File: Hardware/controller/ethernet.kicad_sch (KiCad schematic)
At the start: 33 parts

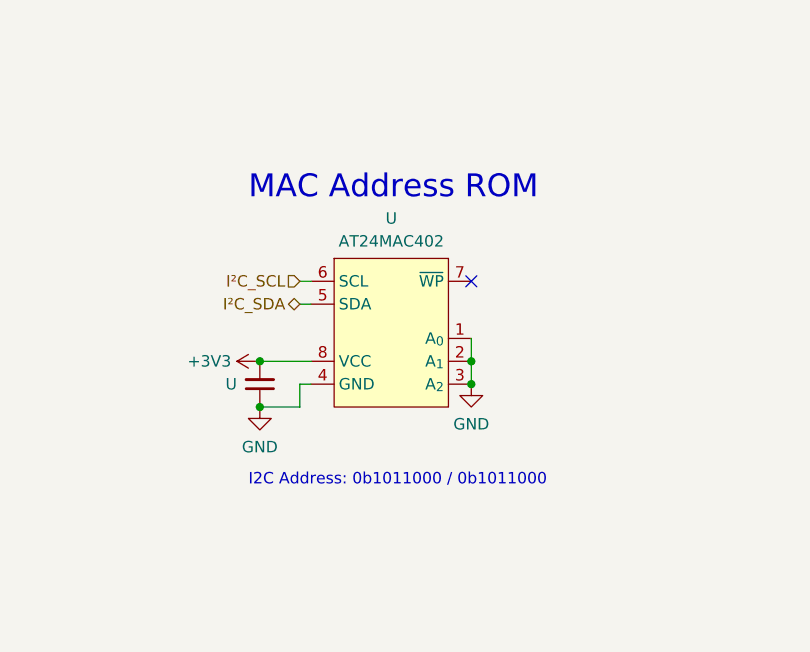
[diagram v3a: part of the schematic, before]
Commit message: hw: start working on rev4 controller
- removed SPI for display, and the associated SPI mux nonsense, and any
  superfluous resistors for pull-ups

- removed MAC address EEPROM

- start adding i2c RTC (which will also contain EEPROM with the MAC of
  the system, lol)

- start moving some components from bottom to top side of board

- tweaked positions of some mains voltage traces

- increased values of power indicator LED's current dropping resistors

- take 3V3 from SoM rather than generate it ourselves
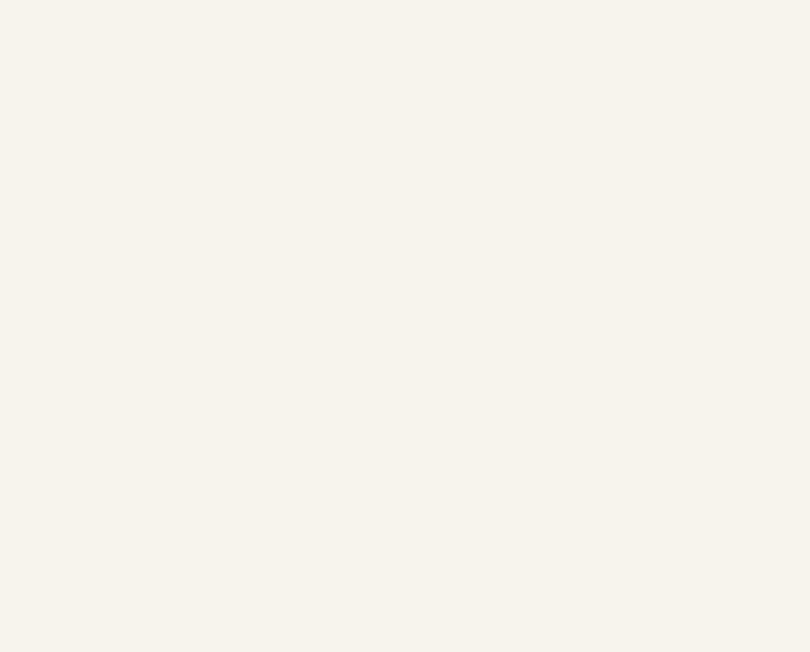
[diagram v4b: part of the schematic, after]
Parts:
- removed U: (no value), symbol Device:C_Small
- removed U: AT24MAC402, Package_SO:TSSOP-8_4.4x3mm_P0.65mm, symbol programmable-load:AT24MAC402
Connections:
- no-connect marks 2 -> 1
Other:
- note removed: "I2C Address: 0b1011000 / 0b1011000"
- note removed: "MAC Address ROM"
- title: (none) -> Programmable Load Controller
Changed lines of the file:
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@@
 (kicad_sch (version 20220404) (generator eeschema)
   (paper "A4")
+  (title_block
+    (title "Programmable Load Controller")
+    (date "2022-06-28")
+    (rev "4")
+  )
   (junction (at 34.29 175.26) (diameter 0) (color 0 0 0 0)
   )
@@
   (junction (at 42.545 125.095) (diameter 0) (color 0 0 0 0)
   )
-  (junction (at 185.42 144.78) (diameter 0) (color 0 0 0 0)
-  )
   (junction (at 89.535 171.45) (diameter 0) (color 0 0 0 0)
   )
@@
   (junction (at 52.705 125.095) (diameter 0) (color 0 0 0 0)
   )
-  (junction (at 208.915 147.32) (diameter 0) (color 0 0 0 0)
-  )
-  (junction (at 185.42 149.86) (diameter 0) (color 0 0 0 0)
-  )
   (junction (at 146.05 27.305) (diameter 0) (color 0 0 0 0)
   )
@@
   (junction (at 34.29 183.515) (diameter 0) (color 0 0 0 0)
   )
-  (junction (at 208.915 144.78) (diameter 0) (color 0 0 0 0)
-  )
   (junction (at 219.075 69.215) (diameter 0) (color 0 0 0 0)
   )
@@
   (junction (at 250.19 69.215) (diameter 0) (color 0 0 0 0)
   )
-  (no_connect (at 208.915 135.89))
   (no_connect (at 106.68 83.82))
   (wire (pts (xy 19.05 175.26) (xy 29.21 175.26))
@@
     (stroke (width 0) (type default))
   )
-  (wire (pts (xy 208.915 142.24) (xy 208.915 144.78))
-    (stroke (width 0) (type default))
-  )
   (wire (pts (xy 105.41 66.04) (xy 106.68 66.04))
     (stroke (width 0) (type default))
@@
     (stroke (width 0) (type default))
   )
-  (wire (pts (xy 208.915 144.78) (xy 208.915 147.32))
-    (stroke (width 0) (type default))
-  )
   (wire (pts (xy 75.565 179.07) (xy 89.535 179.07))
     (stroke (width 0) (type default))
@@
     (stroke (width 0) (type default))
   )
-  (wire (pts (xy 189.865 135.89) (xy 191.135 135.89))
-    (stroke (width 0) (type default))
-  )
   (wire (pts (xy 95.885 58.42) (xy 106.68 58.42))
     (stroke (width 0) (type default))
@@
     (stroke (width 0) (type default))
   )
-  (wire (pts (xy 185.42 144.78) (xy 191.135 144.78))
-    (stroke (width 0) (type default))
-  )
   (wire (pts (xy 19.05 118.11) (xy 19.05 116.84))
     (stroke (width 0) (type default))
@@
     (stroke (width 0) (type default))
   )
-  (wire (pts (xy 185.42 149.86) (xy 189.865 149.86))
-    (stroke (width 0) (type default))
-  )
   (wire (pts (xy 105.41 60.96) (xy 106.68 60.96))
     (stroke (width 0) (type default))
@@
     (stroke (width 0) (type default))
   )
-  (wire (pts (xy 189.865 149.86) (xy 189.865 147.32))
-    (stroke (width 0) (type default))
-  )
   (wire (pts (xy 42.545 116.84) (xy 52.705 116.84))
     (stroke (width 0) (type default))
@@
     (stroke (width 0) (type default))
   )
-  (wire (pts (xy 189.865 138.43) (xy 191.135 138.43))
-    (stroke (width 0) (type default))
-  )
   (wire (pts (xy 86.995 55.88) (xy 88.265 55.88))
     (stroke (width 0) (type default))
@@
   )
   (wire (pts (xy 75.565 177.8) (xy 75.565 179.07))
-    (stroke (width 0) (type default))
-  )
-  (wire (pts (xy 189.865 147.32) (xy 191.135 147.32))
     (stroke (width 0) (type default))
   )
@@
     (effects (font (size 2.54 2.54)) (justify left bottom))
   )
-  (text "I2C Address: 0b1011000 / 0b1011000" (at 184.15 158.75 0)
-    (effects (font (size 1.27 1.27)) (justify left bottom))
-  )
-  (text "MAC Address ROM" (at 184.15 127 0)
-    (effects (font (size 2.54 2.54)) (justify left bottom))
-  )
   (text "No resistors needed: have internal 10K pull-ups" (at 104.14 130.175 0)
     (effects (font (size 1.27 1.27)) (justify left bottom))
@@
     (effects (font (size 1.27 1.27)) (justify right))
   )
-  (hierarchical_label "I²C_SCL " (shape input) (at 189.865 135.89 180) (fields_autoplaced)
-    (effects (font (size 1.27 1.27)) (justify right))
-  )
   (hierarchical_label "CLKIN" (shape input) (at 91.44 81.28 180) (fields_autoplaced)
     (effects (font (size 1.27 1.27)) (justify right))
   )
   (hierarchical_label "~{IRQ}" (shape output) (at 105.41 76.2 180) (fields_autoplaced)
-    (effects (font (size 1.27 1.27)) (justify right))
-  )
-  (hierarchical_label "I²C_SDA" (shape bidirectional) (at 189.865 138.43 180) (fields_autoplaced)
     (effects (font (size 1.27 1.27)) (justify right))
   )
@@
     (pin "2")
   )
-  (symbol (lib_id "power:+3V3") (at 185.42 144.78 90) (unit 1)
-    (in_bom yes) (on_board yes)
-    (default_instance (reference "#PWR") (unit 1) (value "+3V3") (footprint ""))
-    (property "Reference" "#PWR" (id 0) (at 189.23 144.78 0)
-      (effects (font (size 1.27 1.27)) hide)
-    )
-    (property "Value" "+3V3" (id 1) (at 182.245 144.78 90)
-      (effects (font (size 1.27 1.27)) (justify left))
-    )
-    (property "Footprint" "" (id 2) (at 185.42 144.78 0)
-      (effects (font (size 1.27 1.27)) hide)
-    )
-    (property "Datasheet" "" (id 3) (at 185.42 144.78 0)
-      (effects (font (size 1.27 1.27)) hide)
-    )
-    (pin "1")
-  )
   (symbol (lib_id "Device:R_Small") (at 31.75 191.135 90) (unit 1)
     (in_bom yes) (on_board yes)
@@
     (pin "2")
   )
-  (symbol (lib_id "Device:C_Small") (at 185.42 147.32 0) (mirror x) (unit 1)
-    (in_bom yes) (on_board yes)
-    (default_instance (reference "U") (unit 1) (value "") (footprint ""))
-    (property "Reference" "U" (id 0) (at 182.88 147.32 0)
-      (effects (font (size 1.27 1.27)) (justify right))
-    )
-    (property "Value" "" (id 1) (at 182.88 149.86 0)
-      (effects (font (size 1.27 1.27)) (justify right))
-    )
-    (property "Footprint" "" (id 2) (at 185.42 147.32 0)
-      (effects (font (size 1.27 1.27)) hide)
-    )
-    (property "Datasheet" "~" (id 3) (at 185.42 147.32 0)
-      (effects (font (size 1.27 1.27)) hide)
-    )
-    (property "MPN" "" (id 4) (at 185.42 147.32 0)
-      (effects (font (size 1.27 1.27)) hide)
-    )
-    (pin "1")
-    (pin "2")
-  )
   (symbol (lib_id "Device:C_Small") (at 221.615 60.325 90) (unit 1)
     (in_bom yes) (on_board yes) (fields_autoplaced)
@@
     (pin "1")
   )
-  (symbol (lib_id "programmable-load:AT24MAC402") (at 200.025 133.35 0) (unit 1)
-    (in_bom yes) (on_board yes)
-    (default_instance (reference "U") (unit 1) (value "AT24MAC402") (footprint "Package_SO:TSSOP-8_4.4x3mm_P0.65mm"))
-    (property "Reference" "U" (id 0) (at 200.025 128.905 0)
-      (effects (font (size 1.27 1.27)))
-    )
-    (property "Value" "AT24MAC402" (id 1) (at 200.025 131.445 0)
-      (effects (font (size 1.27 1.27)))
-    )
-    (property "Footprint" "Package_SO:TSSOP-8_4.4x3mm_P0.65mm" (id 2) (at 200.025 124.46 0)
-      (effects (font (size 1.27 1.27)) hide)
-    )
-    (property "Datasheet" "https://www.mouser.com/datasheet/2/268/Atmel_8807_SEEPROM_AT24MAC402_602_Datasheet-1368957.pdf" (id 3) (at 200.025 127 0)
-      (effects (font (size 1.27 1.27)) hide)
-    )
-    (property "MPN" "AT24MAC402-XHM-T" (id 4) (at 200.025 133.35 0)
-      (effects (font (size 1.27 1.27)) hide)
-    )
-    (pin "1")
-    (pin "2")
-    (pin "3")
-    (pin "4")
-    (pin "5")
-    (pin "6")
-    (pin "7")
-    (pin "8")
-  )
   (symbol (lib_id "programmable-load:+3V3A") (at 19.05 116.84 0) (unit 1)
     (in_bom yes) (on_board yes)
@@
     (pin "1")
     (pin "2")
-  )
-  (symbol (lib_id "power:GND") (at 185.42 149.86 0) (unit 1)
-    (in_bom yes) (on_board yes)
-    (default_instance (reference "#PWR") (unit 1) (value "GND") (footprint ""))
-    (property "Reference" "#PWR" (id 0) (at 185.42 156.21 0)
-      (effects (font (size 1.27 1.27)) hide)
-    )
-    (property "Value" "GND" (id 1) (at 185.42 154.305 0)
-      (effects (font (size 1.27 1.27)))
-    )
-    (property "Footprint" "" (id 2) (at 185.42 149.86 0)
-      (effects (font (size 1.27 1.27)) hide)
-    )
-    (property "Datasheet" "" (id 3) (at 185.42 149.86 0)
-      (effects (font (size 1.27 1.27)) hide)
-    )
-    (pin "1")
   )
   (symbol (lib_id "Device:R_Small") (at 247.65 38.735 270) (mirror x) (unit 1)
@@
     (pin "5")
   )
-  (symbol (lib_id "power:GND") (at 208.915 147.32 0) (unit 1)
-    (in_bom yes) (on_board yes)
-    (default_instance (reference "#PWR") (unit 1) (value "GND") (footprint ""))
-    (property "Reference" "#PWR" (id 0) (at 208.915 153.67 0)
-      (effects (font (size 1.27 1.27)) hide)
-    )
-    (property "Value" "GND" (id 1) (at 208.915 151.765 0)
-      (effects (font (size 1.27 1.27)))
-    )
-    (property "Footprint" "" (id 2) (at 208.915 147.32 0)
-      (effects (font (size 1.27 1.27)) hide)
-    )
-    (property "Datasheet" "" (id 3) (at 208.915 147.32 0)
-      (effects (font (size 1.27 1.27)) hide)
-    )
-    (pin "1")
-  )
   (symbol (lib_id "power:GND") (at 146.05 33.655 0) (unit 1)

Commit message: hw: add charger for RTC
- added RTC supercapacitor

- added the charging circuit for the RTC (with adjustment for voltage
  and all that fun stuff) based around a bonus linear regulator for the
  supercap

- minor tweaks all around: add more JLCPCB part numbers and fixed some
  footprints for some components
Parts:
- R: JLCPCB (none) -> C25804
- R: JLCPCB (none) -> C23140
- U: JLCPCB (none) -> C4190
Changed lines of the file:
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@@
+      (effects (font (size 1.27 1.27)) hide)
+    )
+    (property "JLCPCB" "C25804" (id 4) (at 31.75 191.135 90)
       (effects (font (size 1.27 1.27)) hide)
     )
@@
       (effects (font (size 1.27 1.27)) hide)
     )
+    (property "JLCPCB" "C25804" (id 4) (at 111.76 123.19 90)
+      (effects (font (size 1.27 1.27)) hide)
+    )
     (pin "1")
     (pin "2")
@@
     )
     (property "Datasheet" "~" (id 3) (at 95.25 81.28 0)
+      (effects (font (size 1.27 1.27)) hide)
+    )
+    (property "JLCPCB" "C23140" (id 4) (at 95.25 81.28 90)
       (effects (font (size 1.27 1.27)) hide)
     )
@@
       (effects (font (size 1.27 1.27)) hide)
     )
+    (property "JLCPCB" "C4190" (id 5) (at 31.75 183.515 90)
+      (effects (font (size 1.27 1.27)) hide)
+    )
     (pin "1")
     (pin "2")
@@
       (effects (font (size 1.27 1.27)) hide)
     )
+    (property "JLCPCB" "C4190" (id 5) (at 31.75 175.26 90)
+      (effects (font (size 1.27 1.27)) hide)
+    )

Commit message: hw: add more part numbers, cleanup
- Added JLCPCB part numbers for more passive components

- Added a status LED for the rear of the board (next to the device USB
  port)
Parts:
- C: JLCPCB (none) -> C15849
- C: JLCPCB (none) -> C1653
- C: JLCPCB (none) -> C57112
- C: JLCPCB (none) -> C1620
- R: JLCPCB (none) -> C23185
- U: JLCPCB (none) -> C7171
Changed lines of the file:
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@@
+      (effects (font (size 1.27 1.27)) hide)
+    )
+    (property "JLCPCB" "C7171" (id 5) (at 89.535 175.26 0)
       (effects (font (size 1.27 1.27)) hide)
     )
@@
     )
     (property "MPN" "CL10B105KP8NFNC" (id 4) (at 158.75 29.845 0)
+      (effects (font (size 1.27 1.27)) hide)
+    )
+    (property "JLCPCB" "C15849" (id 5) (at 158.75 29.845 0)
       (effects (font (size 1.27 1.27)) hide)
     )
@@
       (effects (font (size 1.27 1.27)) hide)
     )
+    (property "JLCPCB" "C1653" (id 4) (at 247.65 60.325 90)
+      (effects (font (size 1.27 1.27)) hide)
+    )
     (pin "1")
     (pin "2")
@@
       (effects (font (size 1.27 1.27)) hide)
     )
+    (property "JLCPCB" "C23185" (id 5) (at 221.615 46.355 90)
+      (effects (font (size 1.27 1.27)) hide)
+    )
     (pin "1")
     (pin "2")
@@
       (effects (font (size 1.27 1.27)) hide)
     )
+    (property "JLCPCB" "C23185" (id 5) (at 247.65 46.355 90)
+      (effects (font (size 1.27 1.27)) hide)
+    )
     (pin "1")
     (pin "2")
@@
     )
     (property "MPN" "TAJA106K016RNJ" (id 4) (at 75.565 175.26 0)
+      (effects (font (size 1.27 1.27)) hide)
+    )
+    (property "JLCPCB" "C7171" (id 5) (at 75.565 175.26 0)
       (effects (font (size 1.27 1.27)) hide)
     )
@@
       (effects (font (size 1.27 1.27)) hide)
     )
+    (property "JLCPCB" "C57112" (id 5) (at 42.545 121.285 0)
+      (effects (font (size 1.27 1.27)) hide)
+    )
     (pin "1")
     (pin "2")
@@
     )
     (property "MPN" "0603B103K500CT" (id 4) (at 29.21 120.65 0)
+      (effects (font (size 1.27 1.27)) hide)
+    )
+    (property "JLCPCB" "C57112" (id 5) (at 29.21 120.65 0)
       (effects (font (size 1.27 1.27)) hide)
     )
@@
     )
     (property "Datasheet" "~" (id 3) (at 221.615 60.325 0)
+      (effects (font (size 1.27 1.27)) hide)
+    )
+    (property "JLCPCB" "C1653" (id 4) (at 221.615 60.325 90)
       (effects (font (size 1.27 1.27)) hide)
     )
@@
       (effects (font (size 1.27 1.27)) hide)
     )
+    (property "JLCPCB" "C57112" (id 5) (at 19.05 120.65 0)
+      (effects (font (size 1.27 1.27)) hide)
+    )
     (pin "1")
     (pin "2")
@@
       (effects (font (size 1.27 1.27)) hide)
     )
+    (property "JLCPCB" "C1653" (id 4) (at 247.65 69.215 90)
+      (effects (font (size 1.27 1.27)) hide)
+    )
     (pin "1")
     (pin "2")
@@
       (effects (font (size 1.27 1.27)) hide)
     )
+    (property "JLCPCB" "C23185" (id 5) (at 247.65 38.735 90)
+      (effects (font (size 1.27 1.27)) hide)
+    )
     (pin "1")
     (pin "2")
@@
       (effects (font (size 1.27 1.27)) hide)
     )
+    (property "JLCPCB" "C1653" (id 4) (at 221.615 69.215 90)
+      (effects (font (size 1.27 1.27)) hide)
+    )
     (pin "1")
     (pin "2")
@@
     )
     (property "MPN" "0603B103K500CT" (id 4) (at 52.705 121.285 0)
+      (effects (font (size 1.27 1.27)) hide)
+    )
+    (property "JLCPCB" "C57112" (id 5) (at 52.705 121.285 0)
       (effects (font (size 1.27 1.27)) hide)
     )
@@
     )
     (property "MPN" "RC0603FR-1049R9L" (id 4) (at 221.615 38.735 0)
+      (effects (font (size 1.27 1.27)) hide)
+    )
+    (property "JLCPCB" "C23185" (id 5) (at 221.615 38.735 90)
       (effects (font (size 1.27 1.27)) hide)
     )
@@
       (effects (font (size 1.27 1.27)) hide)
     )
+    (property "JLCPCB" "C57112" (id 5) (at 62.865 121.285 0)
+      (effects (font (size 1.27 1.27)) hide)
+    )
     (pin "1")
     (pin "2")
@@
       (effects (font (size 1.27 1.27)) hide)
     )
+    (property "JLCPCB" "C1620" (id 5) (at 146.05 29.845 0)
+      (effects (font (size 1.27 1.27)) hide)
+    )

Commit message: hw: fix part numbers
- fixed missing or incorrect MPN and JLCPCB part numbers for various
  components; most should have either one of these now
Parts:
- RN: JLCPCB (none) -> C25508
- U: JLCPCB (none) -> C45223
- U: JLCPCB (none) -> C1015
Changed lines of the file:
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@@
+      (effects (font (size 1.27 1.27)) hide)
+    )
+    (property "JLCPCB" "C45223" (id 4) (at 127 63.5 0)
       (effects (font (size 1.27 1.27)) hide)
     )
@@
       (effects (font (size 1.27 1.27)) hide)
     )
+    (property "JLCPCB" "C25508" (id 4) (at 92.075 50.8 90)
+      (effects (font (size 1.27 1.27)) hide)
+    )
     (pin "1")
     (pin "8")
@@
       (effects (font (size 1.27 1.27)) hide)
     )
+    (property "JLCPCB" "C1015" (id 5) (at 82.55 171.45 90)
+      (effects (font (size 1.27 1.27)) hide)
+    )
     (pin "1")
     (pin "2")
@@
     )
     (property "Datasheet" "~" (id 3) (at 92.075 53.34 0)
+      (effects (font (size 1.27 1.27)) hide)
+    )
+    (property "JLCPCB" "C25508" (id 4) (at 92.075 50.8 90)
       (effects (font (size 1.27 1.27)) hide)
     )
@@
       (effects (font (size 1.27 1.27)) hide)
     )
+    (property "JLCPCB" "C25508" (id 4) (at 92.075 50.8 90)
+      (effects (font (size 1.27 1.27)) hide)
+    )
     (pin "1")
     (pin "8")
@@
       (effects (font (size 1.27 1.27)) hide)
     )
+    (property "JLCPCB" "C25508" (id 4) (at 92.075 63.5 90)
+      (effects (font (size 1.27 1.27)) hide)
+    )
     (pin "1")
     (pin "8")
@@
       (effects (font (size 1.27 1.27)) hide)
     )
+    (property "JLCPCB" "C25508" (id 4) (at 92.075 63.5 90)
+      (effects (font (size 1.27 1.27)) hide)
+    )
     (pin "1")
     (pin "8")
@@
       (effects (font (size 1.27 1.27)) hide)
     )
+    (property "JLCPCB" "C25508" (id 4) (at 92.075 63.5 90)
+      (effects (font (size 1.27 1.27)) hide)
+    )
